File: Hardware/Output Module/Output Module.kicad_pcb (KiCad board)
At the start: 2 copper layers, 41.9 x 31.5 mm, 16 parts, among them J1 Conn_01x12_Male, J2 Conn_01x03_Male, J3 Screw_Terminal_01x02, J4 Screw_Terminal_01x08, Q1 NCV8403A, Q2 NCV8403A, Q3 NCV8403A, Q4 NCV8403A

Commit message: Gerber Upload Ordered version
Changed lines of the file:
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@@
       (layerselection 0x00010fc_ffffffff)
       (disableapertmacros false)
-      (usegerberextensions false)
-      (usegerberattributes true)
-      (usegerberadvancedattributes true)
-      (creategerberjobfile true)
+      (usegerberextensions true)
+      (usegerberattributes false)
+      (usegerberadvancedattributes false)
+      (creategerberjobfile false)
       (svguseinch false)
       (svgprecision 6)
@@
       (psa4output false)
       (plotreference true)
-      (plotvalue true)
+      (plotvalue false)
       (plotinvisibletext false)
       (sketchpadsonfab false)
-      (subtractmaskfromsilk false)
+      (subtractmaskfromsilk true)
       (outputformat 1)
       (mirror false)
-      (drillshape 1)
+      (drillshape 0)
       (scaleselection 1)
-      (outputdirectory "")
+      (outputdirectory "/gerber")
     )
   )
@@
     (effects (font (size 1.5 1.5) (thickness 0.3)))
   )
-  (gr_text "Vext" (at 140.462 80.899) (layer "F.SilkS")
+  (gr_text "Vext" (at 141 80 90) (layer "F.SilkS")
     (effects (font (size 1 1) (thickness 0.1)))
   )
@@
     (effects (font (size 1.5 1.5) (thickness 0.3)))
   )
-  (gr_text "Vmot" (at 140.843 73.279) (layer "F.SilkS")
+  (gr_text "Vmot" (at 141 76 90) (layer "F.SilkS")
     (effects (font (size 1 1) (thickness 0.1)))
   )

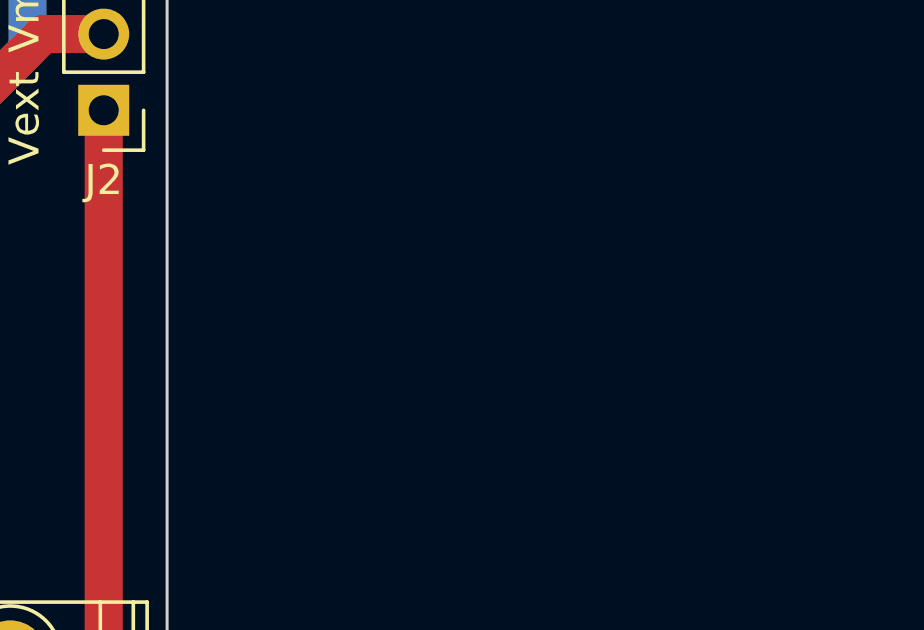
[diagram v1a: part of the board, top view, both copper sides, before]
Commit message: update footprints, cad model for plastic clip
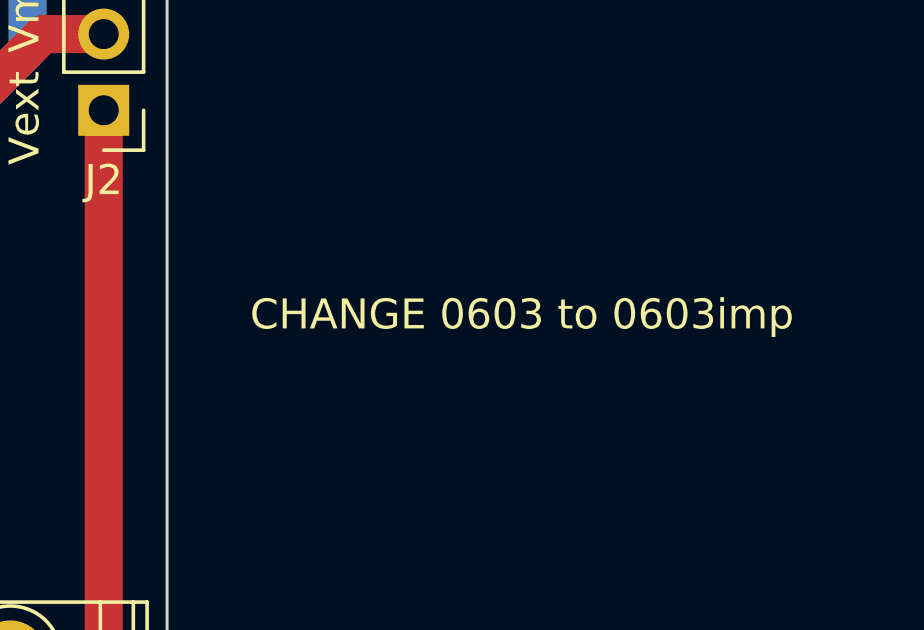
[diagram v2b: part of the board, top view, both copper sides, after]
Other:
- board text added: "CHANGE 0603 to 0603imp"
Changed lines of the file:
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@@
     (effects (font (size 1.5 1.5) (thickness 0.3)))
+  )
+  (gr_text "CHANGE 0603 to 0603imp" (at 157.58 86.55) (layer "F.SilkS")
+    (effects (font (size 1 1) (thickness 0.15)))
   )
   (gr_text "Vmot" (at 141 76 90) (layer "F.SilkS")

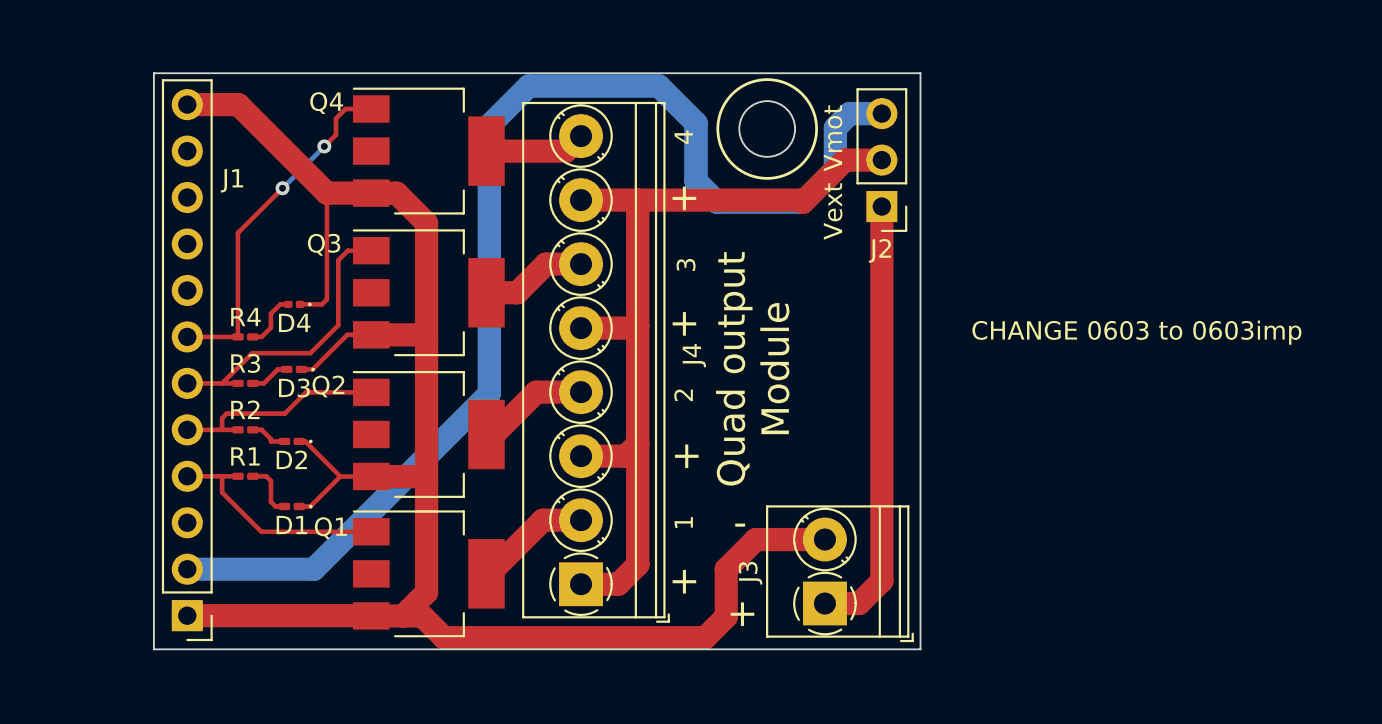
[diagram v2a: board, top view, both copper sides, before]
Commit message: redesigned input and output modules, cleaned some files, ordered 10 of each
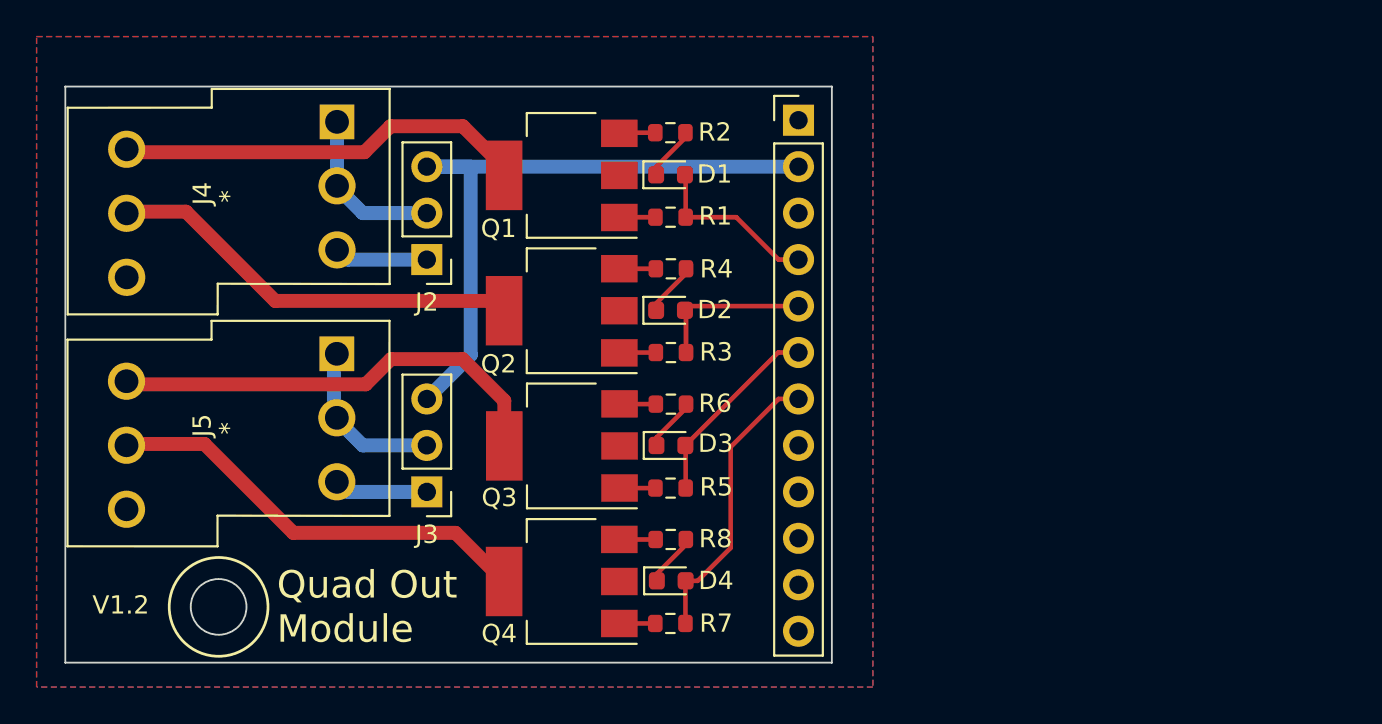
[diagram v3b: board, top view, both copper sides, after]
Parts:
- added J5: Screw_Terminal_01x06, KiCad:2x3 screw terminal3.5mm, F.Cu at (102.3, 89.3)
- added R5: 300, Resistor_SMD:R_0603_1608Metric, F.Cu at (132.1, 95.1)
- added R6: 300, Resistor_SMD:R_0603_1608Metric, F.Cu at (132.1, 90.5)
- added R7: 300, Resistor_SMD:R_0603_1608Metric, F.Cu at (132.1, 102.5)
- added R8: 300, Resistor_SMD:R_0603_1608Metric, F.Cu at (132.1, 97.9)
- D1: footprint LED_SMD:LED_0201_0603Metric_Pad0.64x0.40mm_HandSolder -> LED_SMD:LED_0603_1608Metric
- D2: value LED2 -> LED 1; footprint LED_SMD:LED_0201_0603Metric_Pad0.64x0.40mm_HandSolder -> LED_SMD:LED_0603_1608Metric
- D3: value LED3 -> LED 1; footprint LED_SMD:LED_0201_0603Metric_Pad0.64x0.40mm_HandSolder -> LED_SMD:LED_0603_1608Metric
- D4: value LED4 -> LED 1; footprint LED_SMD:LED_0201_0603Metric -> LED_SMD:LED_0603_1608Metric
- J3: value Screw_Terminal_01x02 -> Conn_01x03_Male; footprint TerminalBlock_Phoenix:TerminalBlock_Phoenix_PT-1,5-2-3.5-H_1x02_P3.50mm_Horizontal -> Connector_PinHeader_2.54mm:PinHeader_1x03_P2.54mm_Vertical
- J4: value Screw_Terminal_01x08 -> Screw_Terminal_01x06; footprint TerminalBlock_Phoenix:TerminalBlock_Phoenix_PT-1,5-8-3.5-H_1x08_P3.50mm_Horizontal -> KiCad:2x3 screw terminal3.5mm
- R1, R2, R3, R4: footprint Resistor_SMD:R_0201_0603Metric_Pad0.64x0.40mm_HandSolder -> Resistor_SMD:R_0603_1608Metric
- moved J1 43.0 mm to (139.1, 75.0), turned to 0 degrees
- moved J4 34.4 mm to (102.3, 76.6), turned to -90 degrees
- moved R2 28.4 mm to (132.1, 75.7), turned to 180 degrees
- moved D1 27.5 mm to (132.1, 78.0), turned to 0 degrees
- moved R1 27.2 mm to (132.1, 80.3), turned to 180 degrees
- moved D4 25.6 mm to (132.1, 100.2), turned to 0 degrees
- moved J2 25.0 mm to (118.8, 82.6)
- moved Q4 24.6 mm to (126.1, 100.2), turned to 180 degrees
- moved R4 23.6 mm to (132.1, 83.1), turned to 180 degrees
- moved R3 23.3 mm to (132.1, 87.7), turned to 180 degrees
- moved Q1 23.0 mm to (126.1, 78.0), turned to 180 degrees
- moved J3 22.6 mm to (118.8, 95.3), turned to 180 degrees
- moved D2 21.9 mm to (132.1, 85.4), turned to 0 degrees
- moved D3 21.0 mm to (132.1, 92.8), turned to 0 degrees
- moved Q3 11.1 mm to (126.1, 92.8), turned to 180 degrees
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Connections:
- D1 pad 1: GND -> Net-(D1-Pad1)
- D1 pad 2: Net-(D1-Pad2) -> GATE 1
- D2 pad 1: GND -> Net-(D2-Pad1)
- D2 pad 2: Net-(D2-Pad2) -> GATE 2
- D3 pad 1: GND -> Net-(D3-Pad1)
- D3 pad 2: Net-(D3-Pad2) -> GATE 3
- D4 pad 1: GND -> Net-(D4-Pad1)
- D4 pad 2: Net-(D4-Pad2) -> GATE 4
- J1 pad 2: Net-(J1-Pad2) -> VMOT
- J1 pad 4: Net-(J1-Pad4) -> GATE 1
- J1 pad 5: Net-(J1-Pad5) -> GATE 2
- J1 pad 6: Net-(J1-Pad6) -> GATE 3
- J1 pad 7: Net-(J1-Pad7) -> GATE 4
- J2 pad 1: Net-(J2-Pad1) -> VEXT 1
- J2 pad 2: Net-(J2-Pad2) -> VOUT 1
- J2 pad 3: Net-(J1-Pad2) -> VMOT
- J3 pad 1: Net-(J2-Pad1) -> VEXT 2
- J3 pad 2: GND -> VOUT 2
- J4 pad 1: Net-(J2-Pad2) -> VOUT 1
- J4 pad 2: Net-(J4-Pad2) -> VOUT 1
- J4 pad 3: Net-(J2-Pad2) -> VEXT 1
- J4 pad 4: Net-(J4-Pad4) -> SINK 1
- J4 pad 5: Net-(J2-Pad2) -> SINK 2
- J4 pad 6: Net-(J4-Pad6) -> GND
- Q1 pad 1: Net-(J1-Pad4) -> Net-(Q1-Pad1)
- Q1 pad 4: Net-(J4-Pad2) -> SINK 1
- Q2 pad 1: Net-(J1-Pad5) -> Net-(Q2-Pad1)
- Q2 pad 4: Net-(J4-Pad4) -> SINK 2
- Q3 pad 1: Net-(J1-Pad6) -> Net-(Q3-Pad1)
- Q3 pad 4: Net-(J4-Pad6) -> SINK 3
- Q4 pad 1: Net-(J1-Pad7) -> Net-(Q4-Pad1)
- Q4 pad 4: Net-(J4-Pad8) -> SINK 4
- R1 pad 1: Net-(J1-Pad4) -> GATE 1
- R1 pad 2: Net-(D1-Pad2) -> Net-(Q1-Pad1)
- R2 pad 1: Net-(J1-Pad5) -> Net-(D1-Pad1)
- R2 pad 2: Net-(D2-Pad2) -> GND
- R3 pad 1: Net-(J1-Pad6) -> GATE 2
- R3 pad 2: Net-(D3-Pad2) -> Net-(Q2-Pad1)
- R4 pad 1: Net-(J1-Pad7) -> Net-(D2-Pad1)
- R4 pad 2: Net-(D4-Pad2) -> GND
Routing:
- net GND: track 102.8 -> 7.95 mm
- net Net-(J1-Pad2): track 65.3 -> 0.00 mm
- net Net-(J2-Pad2): track 47.5 -> 0.00 mm
- net VMOT: track 0.00 -> 36.4 mm
- net SINK 3: track 0.00 -> 24.7 mm
- net Net-(J2-Pad1): track 24.1 -> 0.00 mm
- net SINK 4: track 0.00 -> 23.8 mm
- net SINK 2: track 0.00 -> 22.9 mm
- net SINK 1: track 0.00 -> 22.7 mm
- net Net-(J1-Pad7): track 19.1 -> 0.00 mm, vias 2 -> 0
- net Net-(J1-Pad6): track 16.0 -> 0.00 mm
- net GATE 4: track 0.00 -> 15.9 mm
- net Net-(J1-Pad4): track 12.7 -> 0.00 mm
- net Net-(J1-Pad5): track 12.2 -> 0.00 mm
- net GATE 3: track 0.00 -> 10.6 mm
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- added copper zone on B.Cu, net GND
- added copper zone on F.Cu, net GND
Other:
- outline, holes or cut-outs redrawn
- board text added: "Quad Out Module"
- board text added: "V1.2"
- board text removed: "+"
- board text removed: "-"
- board text removed: "1"
- board text removed: "2"
- board text removed: "3"
- board text removed: "4"
- board text removed: "CHANGE 0603 to 0603imp"
- board text removed: "Quad output Module"
- board text removed: "Vext"
- board text removed: "Vmot"
